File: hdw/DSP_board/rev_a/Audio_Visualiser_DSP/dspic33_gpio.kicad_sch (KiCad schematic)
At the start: 18 parts, among them U701 dsPIC33AK256MPS105, U801 74LVC1G97, U802 PCA9536DP, U803 TCA9803

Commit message: fixed dsPIC pinout to add exposed pad, fixed footprint mapping. Fixed +12V connection to INA
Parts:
- U701: footprint Package_DFN_QFN:QFN-48-1EP_6x6mm_P0.4mm_EP4.1x4.1mm -> Package_DFN_QFN:VQFN-48-1EP_6x6mm_P0.4mm_EP4.1x4.1mm
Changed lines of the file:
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@@
 			)
 		)
-		(property "Footprint" "Package_DFN_QFN:QFN-48-1EP_6x6mm_P0.4mm_EP4.1x4.1mm"
+		(property "Footprint" "Package_DFN_QFN:VQFN-48-1EP_6x6mm_P0.4mm_EP4.1x4.1mm"
 			(at 114.3 53.34 0)
 			(hide yes)
@@
 		(pin "47"
 		)
+		(pin "49"
+		)
 		(instances

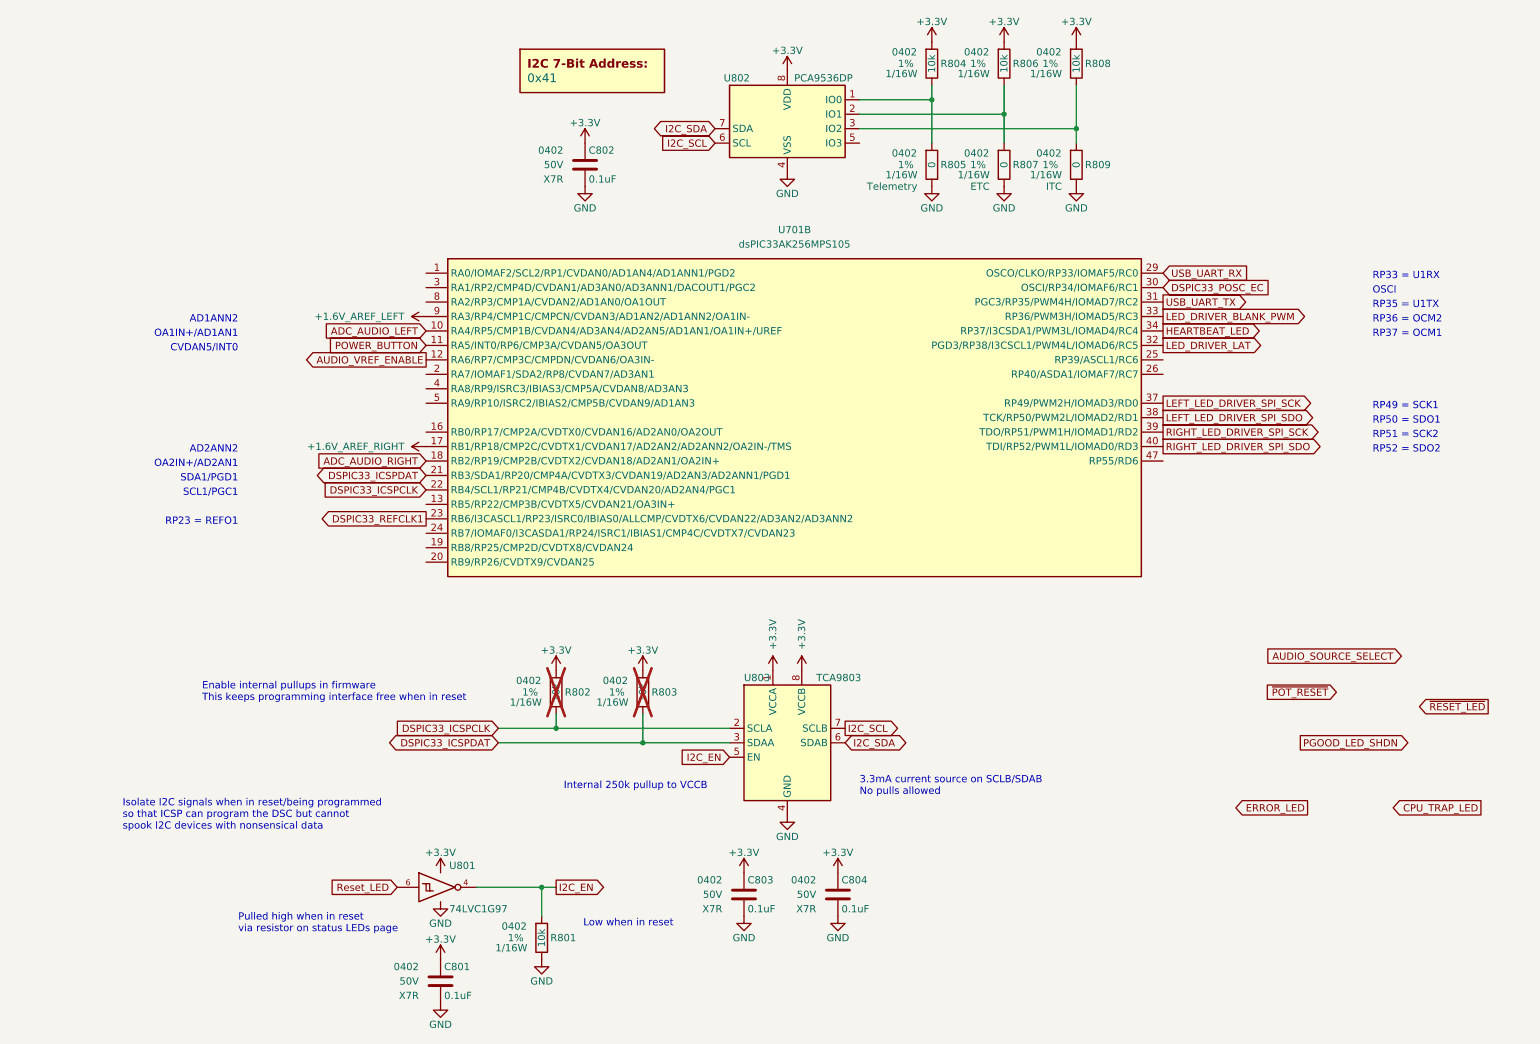
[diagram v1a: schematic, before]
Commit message: Added speaker signal path
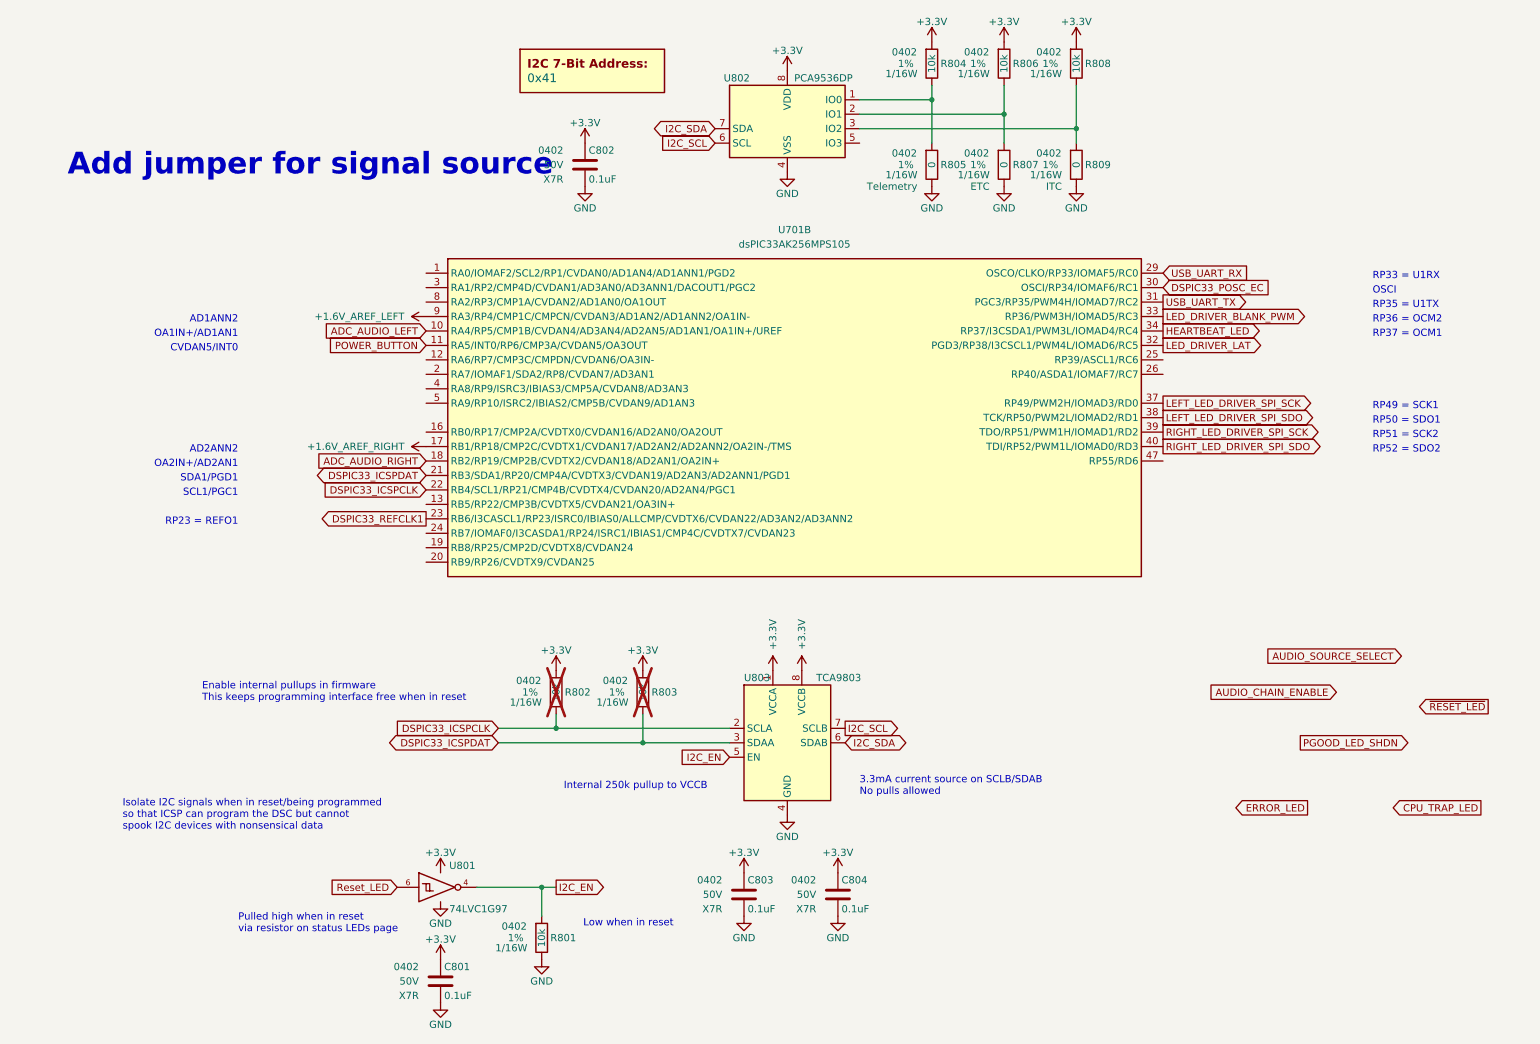
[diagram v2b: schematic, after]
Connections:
- net AUDIO_VREF_ENABLE: no longer names the net of U701.12 (RA6/RP7/CMP3C/CMPDN/CVDAN6/OA3IN-)
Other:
- note added: "Add jumper for signal source"
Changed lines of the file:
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@@
+		)
+	)
+	(text "Add jumper for signal source"
+		(exclude_from_sim no)
+		(at 49.53 41.91 0)
+		(effects
+			(font
+				(size 3.81 3.81)
+				(thickness 0.762)
+				(bold yes)
+				(color 194 0 0 1)
+			)
 		)
 	)
@@
 		)
 	)
-	(global_label "~{POT_RESET}"
+	(global_label "AUDIO_CHAIN_ENABLE"
 		(shape input)
 		(at 229.87 134.62 180)
@@
 		)
 		(property "Intersheetrefs" "${INTERSHEET_REFS}"
-			(at 216.604 134.62 0)
+			(at 206.6856 134.62 0)
 			(hide yes)
 			(show_name no)
@@
 			)
 		)
-	)
-	(global_label "AUDIO_VREF_ENABLE"
-		(shape output)
-		(at 69.85 76.2 180)
-		(fields_autoplaced yes)
-		(effects
-			(font
-				(size 1.27 1.27)
-			)
-			(justify right)
-		)
-		(property "Intersheetrefs" "${INTERSHEET_REFS}"
-			(at 47.6938 76.2 0)
-			(hide yes)
-			(show_name no)
-			(do_not_autoplace no)
-			(effects
-				(font
-					(size 1.27 1.27)
-				)
-				(justify right)
-			)
-		)

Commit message: added buffering for audio enable signal
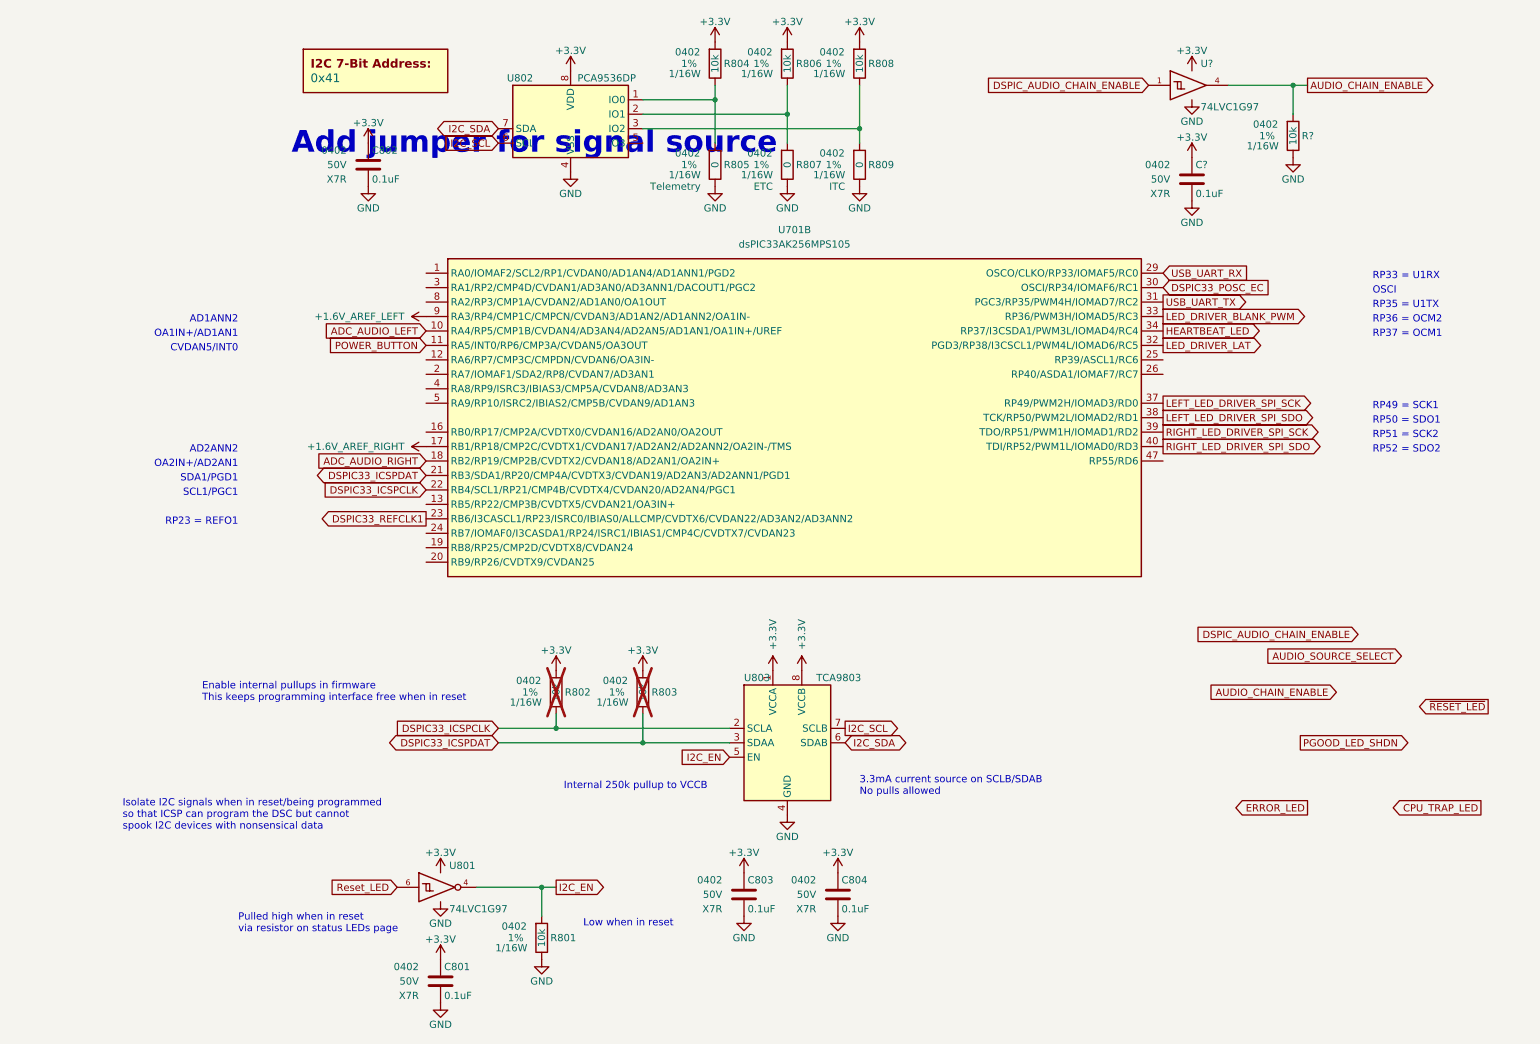
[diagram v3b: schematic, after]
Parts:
- added C?: 0.1uF, Capacitors_SMD:C_0402, symbol Custom_Library:C_Custom
- added R?: 10k, Resistors_SMD:R_0402, symbol Custom_Library:R_Custom
- added U?: 74LVC1G97, Package_TO_SOT_SMD:SOT-363_SC-70-6, symbol Custom Library:74LVC1G97_Power_BUF
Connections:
- net +3.3V: now also C?.1, U?.5 (VCC)
- net AUDIO_CHAIN_ENABLE: now also R?.1, U?.4
- net GND: now also C?.2, R?.2, U?.2 (GND), U?.3 (GND), U?.6 (GND)
- new net DSPIC_AUDIO_CHAIN_ENABLE: U?.1
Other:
- moved on the sheet: C802, R804, R805, R806, R807, R808, R809, U802

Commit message: added LED panel connectors
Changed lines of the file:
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@@
+		)
+	)
+	(global_label "~{LED_BUF_OE}"
+		(shape input)
+		(at 243.84 148.59 0)
+		(fields_autoplaced yes)
+		(effects
+			(font
+				(size 1.27 1.27)
+			)
+			(justify left)
+		)
+		(property "Intersheetrefs" "${INTERSHEET_REFS}"
+			(at 258.3761 148.59 0)
+			(hide yes)
+			(show_name no)
+			(do_not_autoplace no)
+			(effects
+				(font
+					(size 1.27 1.27)
+				)
+				(justify left)
+			)
 		)
 	)

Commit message: add simulation data for speaker input path
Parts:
- gave numbers to parts that had none: 3
- renumbered C802 to C801, C801 to C802, U701 to U804

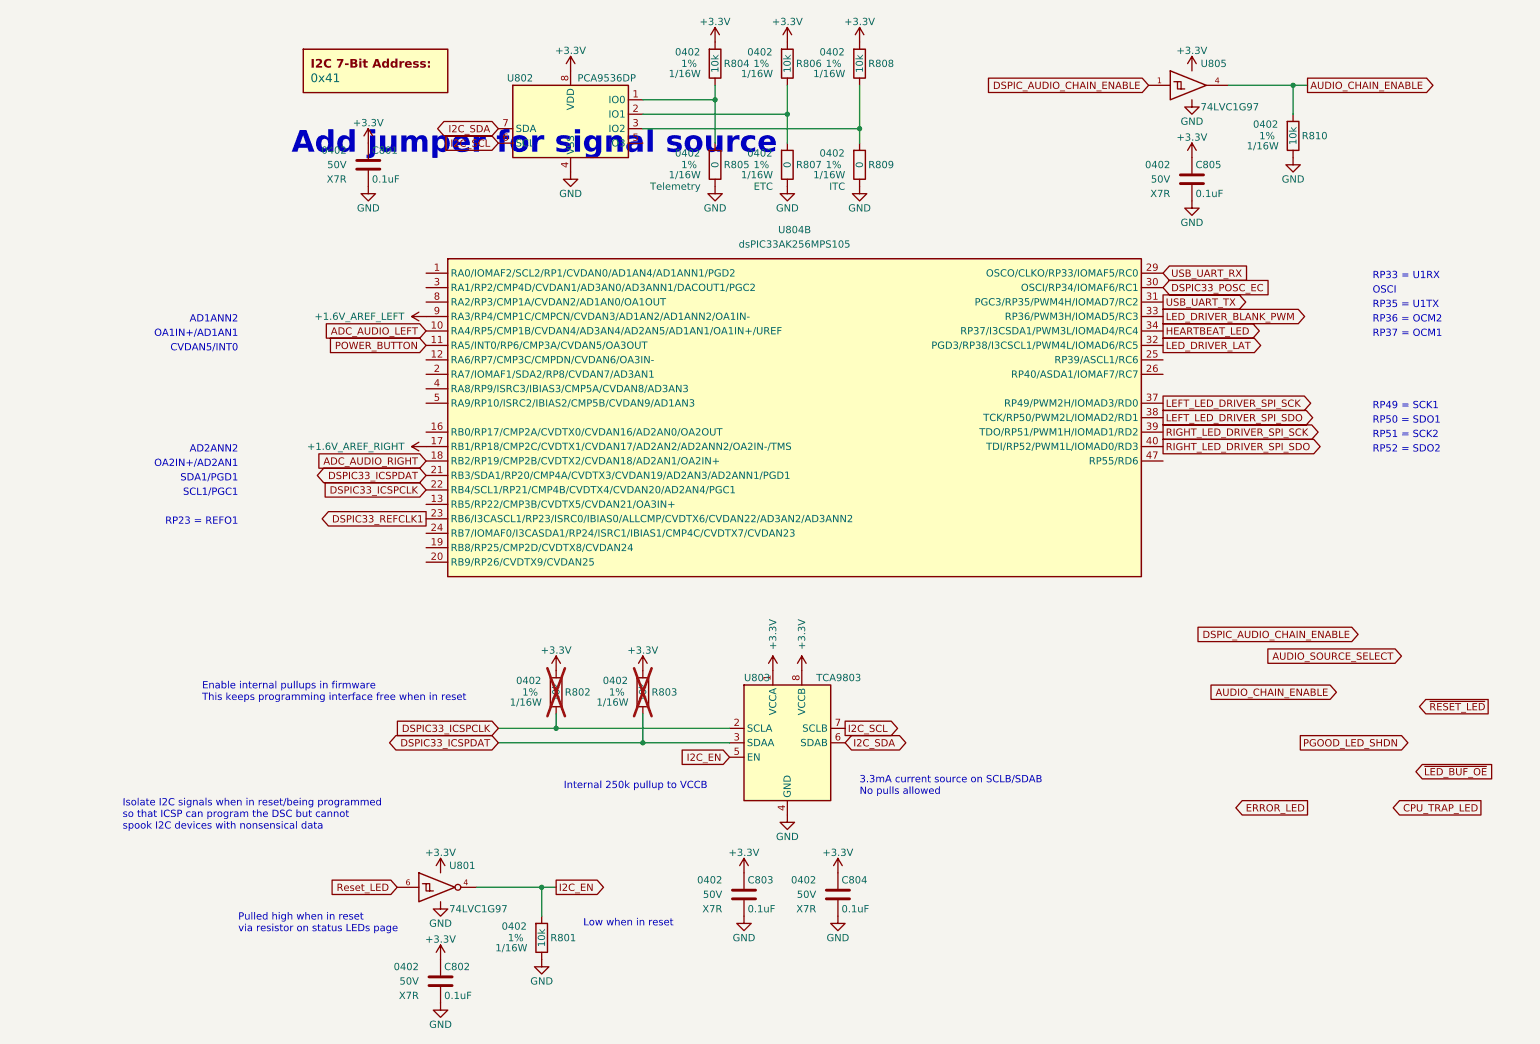
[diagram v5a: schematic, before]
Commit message: Added a bunch of stuff to the schematic
Moved to adafruit I2C rotary encoder module. Added signal test points. Added some design schematic notes. Added LEd output connector ESD diodes. Consolidated on a single schottky diode. Connected most signals to MCU
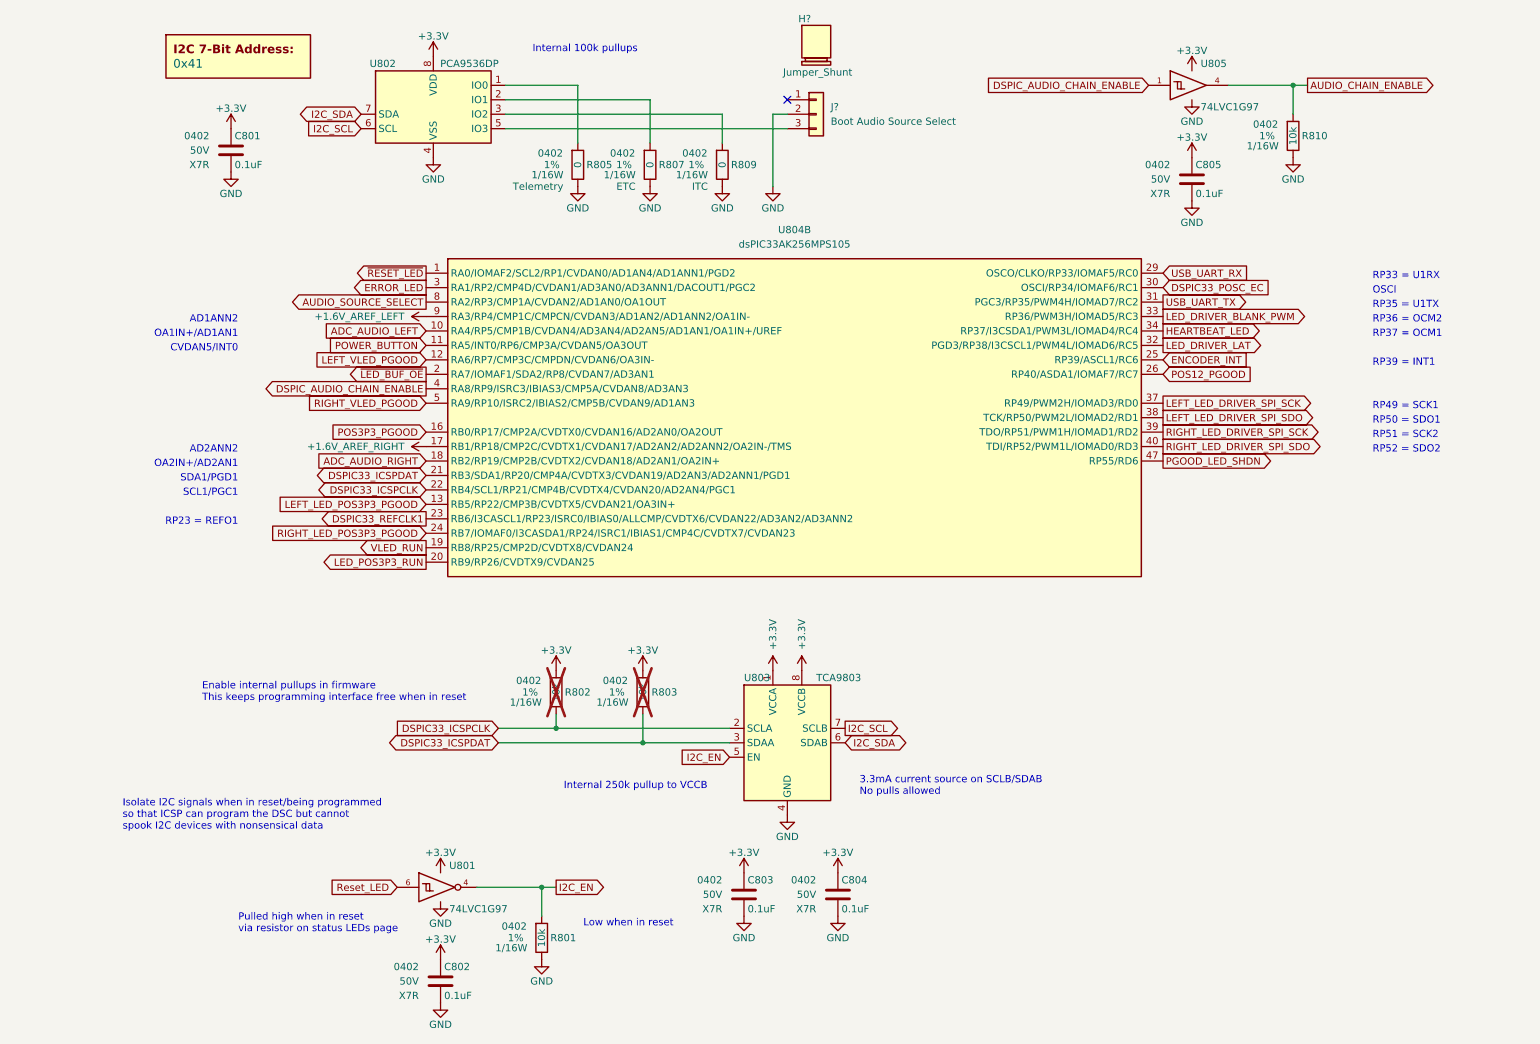
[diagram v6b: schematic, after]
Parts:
- removed R804, R806, R808: 10k, Resistors_SMD:R_0402, symbol Custom_Library:R_Custom
- added H?: Jumper_Shunt, symbol Auxiliary_Items:Jumper_Shunt
- added J?: Boot Audio Source Select, symbol Connector_Generic:Conn_01x03
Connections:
- net AUDIO_SOURCE_SELECT: now also U804.8 (RA2/RP3/CMP1A/CVDAN2/AD1AN0/OA1OUT)
- net DSPIC_AUDIO_CHAIN_ENABLE: now also U804.4 (RA8/RP9/ISRC3/IBIAS3/CMP5A/CVDAN8/AD3AN3)
- net ERROR_LED: now also U804.3 (RA1/RP2/CMP4D/CVDAN1/AD3AN0/AD3ANN1/DACOUT1/PGC2)
- net GND: now also J?.2 (Pin_2)
- net PGOOD_LED_SHDN: now also U804.47 (RP55/RD6)
- net ~{LED_BUF_OE}: now also U804.2 (RA7/IOMAF1/SDA2/RP8/CVDAN7/AD3AN1)
- net ~{RESET_LED}: now also U804.1 (RA0/IOMAF2/SCL2/RP1/CVDAN0/AD1AN4/AD1ANN1/PGD2)
- net LEFT_VLED_PGOOD: now reaches U804.12 (RA6/RP7/CMP3C/CMPDN/CVDAN6/OA3IN-)
- net LEFT_LED_POS3P3_PGOOD: now reaches U804.13 (RB5/RP22/CMP3B/CVDTX5/CVDAN21/OA3IN+)
- net POS3P3_PGOOD: now reaches U804.16 (RB0/RP17/CMP2A/CVDTX0/CVDAN16/AD2AN0/OA2OUT)
- net VLED_RUN: now reaches U804.19 (RB8/RP25/CMP2D/CVDTX8/CVDAN24)
- net LED_POS3P3_RUN: now reaches U804.20 (RB9/RP26/CVDTX9/CVDAN25)
- net RIGHT_LED_POS3P3_PGOOD: now reaches U804.24 (RB7/IOMAF0/I3CASDA1/RP24/ISRC1/IBIAS1/CMP4C/CVDTX7/CVDAN23)
- net ENCODER_INT: now reaches U804.25 (RP39/ASCL1/RC6)
- net POS12_PGOOD: now reaches U804.26 (RP40/ASDA1/IOMAF7/RC7)
- net RIGHT_VLED_PGOOD: now reaches U804.5 (RA9/RP10/ISRC2/IBIAS2/CMP5B/CVDAN9/AD1AN3)
- net at U802.5 (IO3): now also J?.3 (Pin_3)
- no-connect marks 0 -> 1
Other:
- note added: "Internal 100k pullups"
- note added: "RP39 = INT1"
- note removed: "Add jumper for signal source"
- moved on the sheet: C801, R805, R807, R809, U802

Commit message: Added simulation outputs, sim readme
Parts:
- gave numbers to parts that had none: 2
- renumbered R805 to R803, R803 to R804, R807 to R805, R809 to R806, R810 to R807, U804 to U701, U802 to U801, U801 to U802
